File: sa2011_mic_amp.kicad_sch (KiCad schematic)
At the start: 12 parts, among them SW1 SW_SPST, U1 SA2011

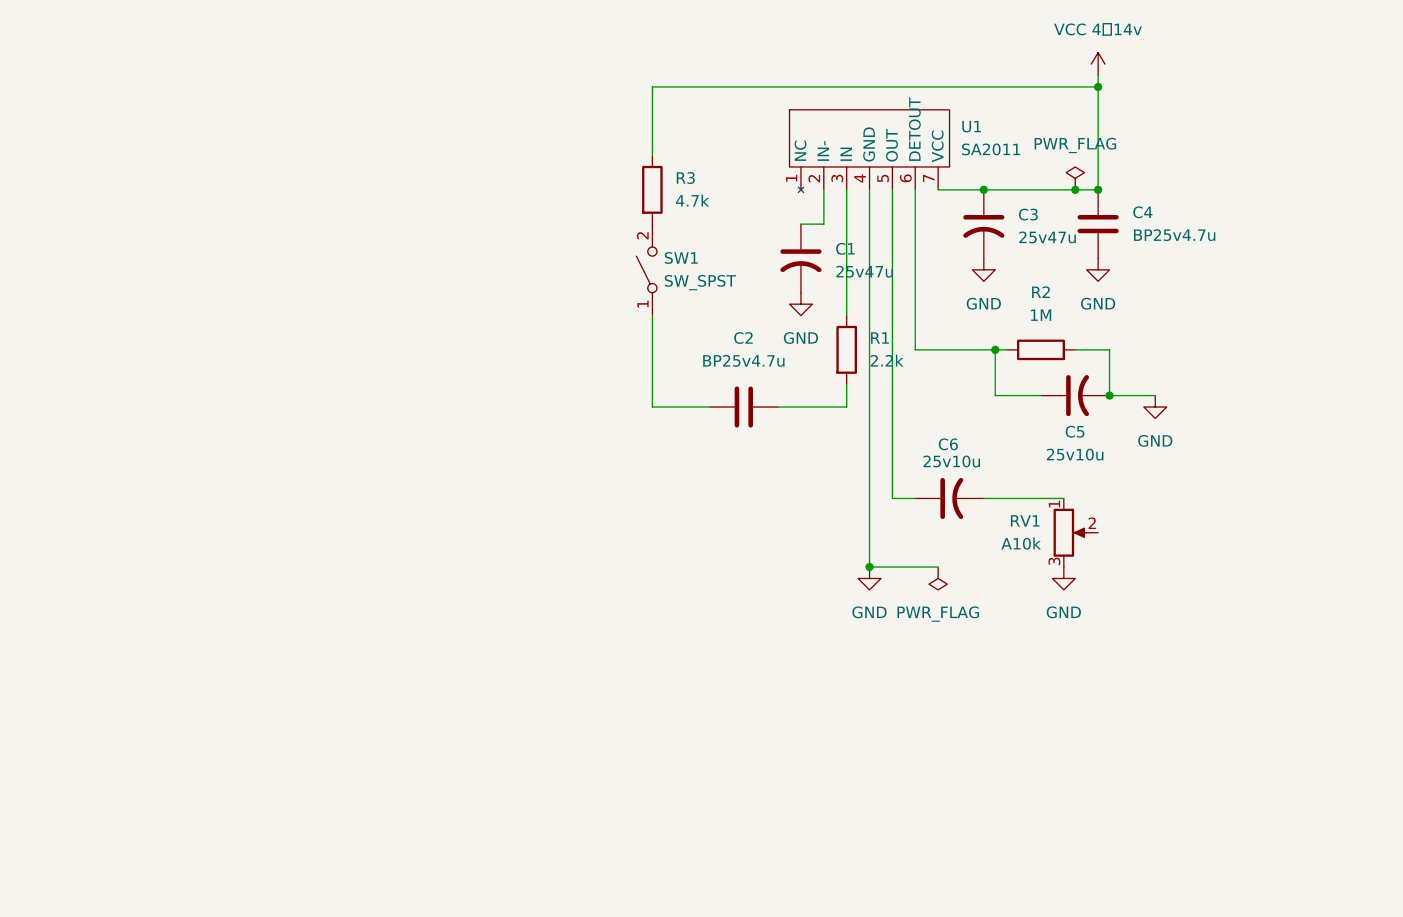
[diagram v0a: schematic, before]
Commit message: ALCを可変抵抗に、EMCとの切り替えスイッチをつけて配置
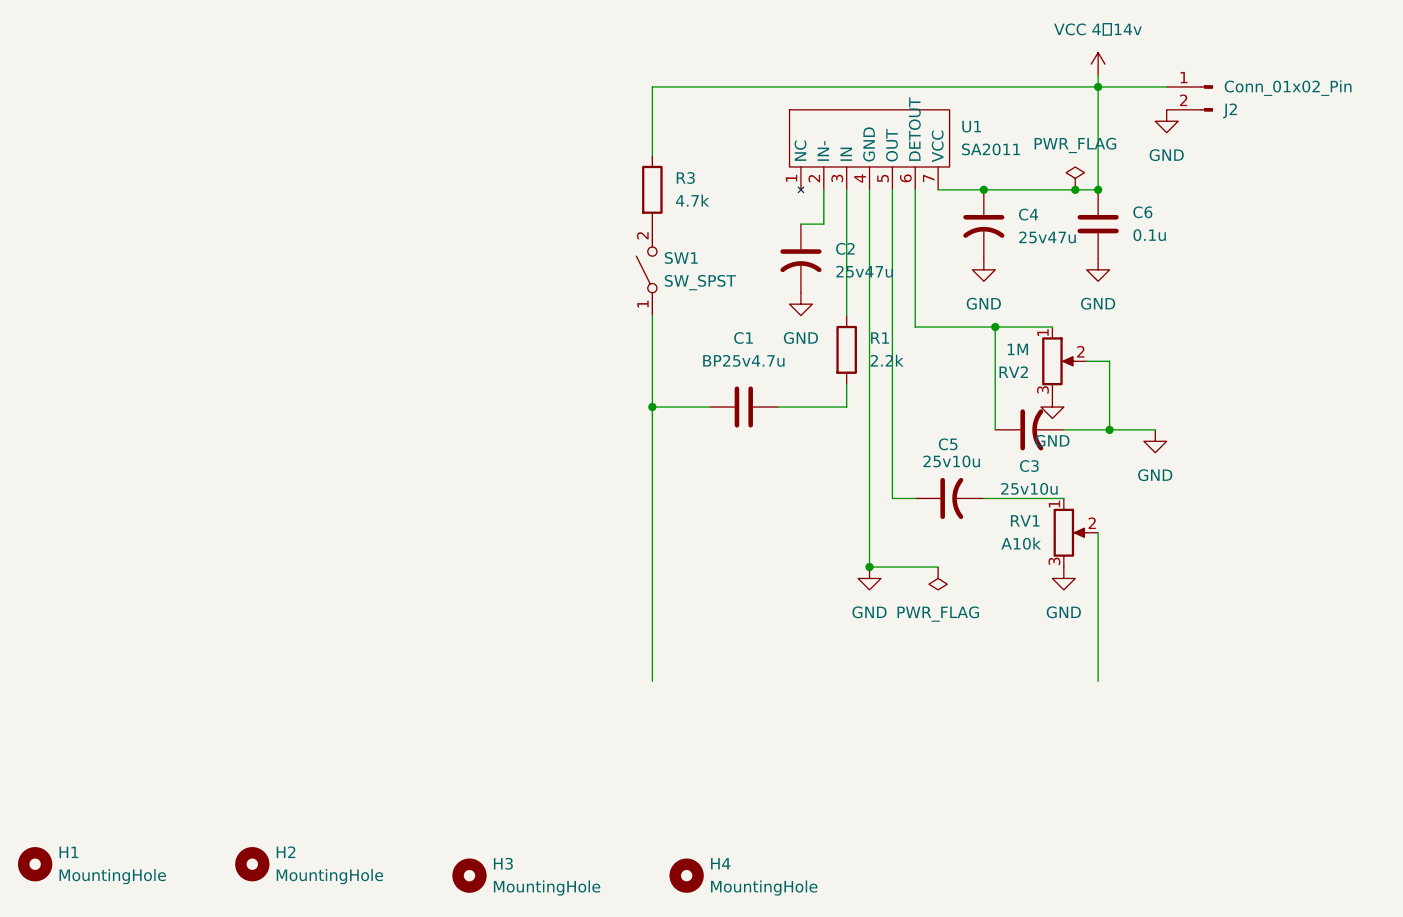
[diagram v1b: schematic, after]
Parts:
- removed R2: 1M, symbol Device:R
- added H1, H2, H3, H4: MountingHole, MountingHole:MountingHole_3.2mm_M3, symbol Mechanical:MountingHole
- added J2: Conn_01x02_Pin, Connector_JST:JST_XH_B2B-XH-A_1x02_P2.50mm_Vertical, symbol Connector:Conn_01x02_Pin
- added RV2: 1M, Potentiometer_THT:Potentiometer_Vishay_T73YP_Vertical, symbol Device:R_Potentiometer
- C1: renamed from C2; footprint (none) -> Capacitor_THT:CP_Radial_D5.0mm_P2.50mm
- C2: renamed from C1; footprint (none) -> Capacitor_THT:CP_Radial_D6.3mm_P2.50mm
- C3: renamed from C5; footprint (none) -> Capacitor_THT:CP_Radial_D5.0mm_P2.50mm
- C4: renamed from C3; footprint (none) -> Capacitor_THT:CP_Radial_D6.3mm_P2.50mm
- C5: renamed from C6; footprint (none) -> Capacitor_THT:CP_Radial_D5.0mm_P2.50mm
- C6: renamed from C4; value BP25v4.7u -> 0.1u; footprint (none) -> Capacitor_THT:C_Disc_D11.0mm_W5.0mm_P5.00mm
- R1, R3: footprint (none) -> Resistor_THT:R_Axial_DIN0207_L6.3mm_D2.5mm_P7.62mm_Horizontal
- SW1: footprint (none) -> Button_Switch_THT:SW_Slide-03_Wuerth-WS-SLTV_10x2.5x6.4_P2.54mm
- U1: footprint (none) -> @MyLibrary:SIP-7_19x3mm_P2.54mm
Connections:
- net GND: now also J2.2 (Pin_2), RV2.2, RV2.3
- net VCC 4～14v: now also J2.1 (Pin_1)
- net at C3.1, U1.6 (DETOUT): now also RV2.1
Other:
- moved on the sheet: C3

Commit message: 縦長に配置を変更
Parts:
- R3: footprint Resistor_THT:R_Axial_DIN0207_L6.3mm_D2.5mm_P7.62mm_Horizontal -> Resistor_THT:R_Axial_DIN0207_L6.3mm_D2.5mm_P2.54mm_Vertical
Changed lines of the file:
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@@
 			)
 		)
-		(property "Footprint" "Resistor_THT:R_Axial_DIN0207_L6.3mm_D2.5mm_P7.62mm_Horizontal"
+		(property "Footprint" "Resistor_THT:R_Axial_DIN0207_L6.3mm_D2.5mm_P2.54mm_Vertical"
 			(at 102.362 83.82 90)
 			(effects

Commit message: 配置を修正
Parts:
- R3: footprint Resistor_THT:R_Axial_DIN0207_L6.3mm_D2.5mm_P2.54mm_Vertical -> Resistor_THT:R_Axial_DIN0207_L6.3mm_D2.5mm_P7.62mm_Horizontal
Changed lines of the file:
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@@
 			)
 		)
-		(property "Footprint" "Resistor_THT:R_Axial_DIN0207_L6.3mm_D2.5mm_P2.54mm_Vertical"
+		(property "Footprint" "Resistor_THT:R_Axial_DIN0207_L6.3mm_D2.5mm_P7.62mm_Horizontal"
 			(at 102.362 83.82 90)
 			(effects
